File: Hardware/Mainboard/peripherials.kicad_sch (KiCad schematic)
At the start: 2 parts, among them J14 Conn_02x03_Odd_Even, J15 Conn_02x03_Odd_Even

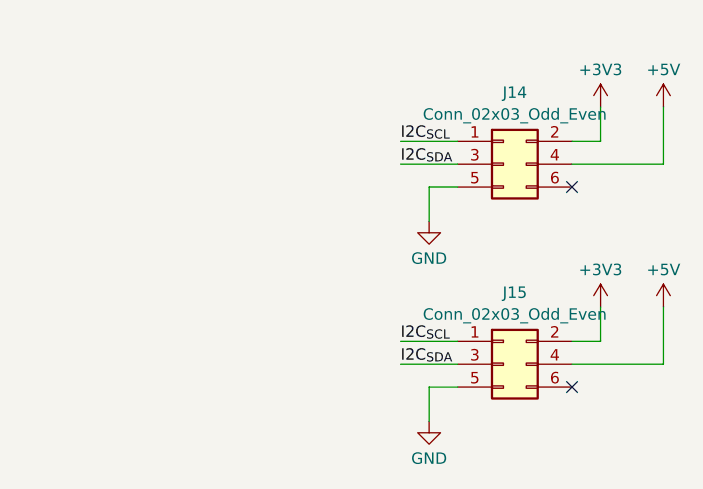
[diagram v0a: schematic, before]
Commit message: Adds more work on the mainboard schematic
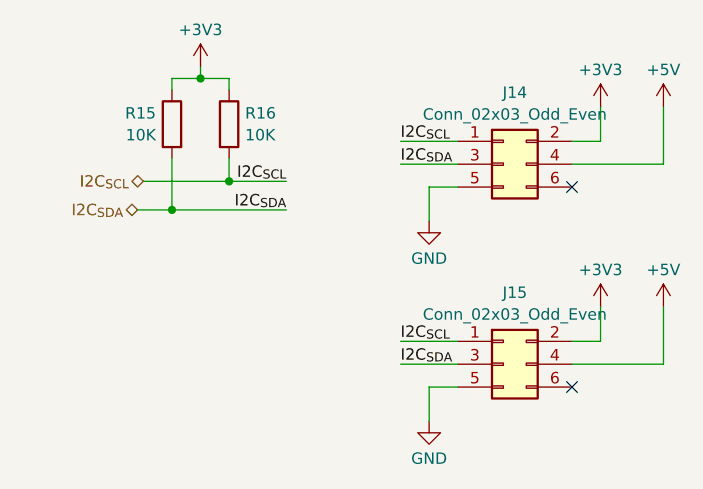
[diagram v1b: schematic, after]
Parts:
- added R15, R16: 10K, Resistor_SMD:R_0603_1608Metric_Pad0.98x0.95mm_HandSolder, symbol Device:R
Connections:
- net +3V3: now also R15.1, R16.1
- net I2C_{SCL}: now also R16.2
- net I2C_{SDA}: now also R15.2
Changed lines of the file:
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@@
 (kicad_sch (version 20230121) (generator eeschema)
   (paper "A4")
+  (junction (at 28.575 25.4) (diameter 0) (color 0 0 0 0)
+  )
+  (junction (at 25.4 40.005) (diameter 0) (color 0 0 0 0)
+  )
+  (junction (at 31.75 36.83) (diameter 0) (color 0 0 0 0)
+  )
   (no_connect (at 69.85 37.465))
   (no_connect (at 69.85 59.69))
@@
     (stroke (width 0) (type default))
   )
+  (wire (pts (xy 25.4 26.67) (xy 25.4 25.4))
+    (stroke (width 0) (type default))
+  )
   (wire (pts (xy 69.85 34.925) (xy 80.01 34.925))
     (stroke (width 0) (type default))
@@
     (stroke (width 0) (type default))
   )
+  (wire (pts (xy 28.575 25.4) (xy 31.75 25.4))
+    (stroke (width 0) (type default))
+  )
+  (wire (pts (xy 31.75 36.83) (xy 38.1 36.83))
+    (stroke (width 0) (type default))
+  )
   (wire (pts (xy 57.15 37.465) (xy 53.975 37.465))
     (stroke (width 0) (type default))
@@
     (stroke (width 0) (type default))
   )
+  (wire (pts (xy 25.4 25.4) (xy 28.575 25.4))
+    (stroke (width 0) (type default))
+  )
+  (wire (pts (xy 31.75 34.29) (xy 31.75 36.83))
+    (stroke (width 0) (type default))
+  )
   (wire (pts (xy 80.01 50.8) (xy 80.01 57.15))
     (stroke (width 0) (type default))
   )
+  (wire (pts (xy 28.575 24.13) (xy 28.575 25.4))
+    (stroke (width 0) (type default))
+  )
+  (wire (pts (xy 25.4 40.005) (xy 38.1 40.005))
+    (stroke (width 0) (type default))
+  )
+  (wire (pts (xy 25.4 34.29) (xy 25.4 40.005))
+    (stroke (width 0) (type default))
+  )
   (wire (pts (xy 50.8 54.61) (xy 57.15 54.61))
     (stroke (width 0) (type default))
@@
     (stroke (width 0) (type default))
   )
+  (wire (pts (xy 22.225 36.83) (xy 31.75 36.83))
+    (stroke (width 0) (type default))
+  )
   (wire (pts (xy 69.85 32.385) (xy 73.025 32.385))
     (stroke (width 0) (type default))
@@
   (wire (pts (xy 69.85 54.61) (xy 73.025 54.61))
     (stroke (width 0) (type default))
+  )
+  (wire (pts (xy 31.75 26.67) (xy 31.75 25.4))
+    (stroke (width 0) (type default))
+  )
+  (wire (pts (xy 21.59 40.005) (xy 25.4 40.005))
+    (stroke (width 0) (type default))
+  )
+  (label "I2C_{SCL}" (at 38.1 36.83 180) (fields_autoplaced)
+    (effects (font (size 1.27 1.27)) (justify right bottom))
   )
   (label "I2C_{SCL}" (at 50.8 32.385 0) (fields_autoplaced)
@@
     (effects (font (size 1.27 1.27)) (justify left bottom))
   )
+  (label "I2C_{SDA}" (at 38.1 40.005 180) (fields_autoplaced)
+    (effects (font (size 1.27 1.27)) (justify right bottom))
+  )
   (label "I2C_{SCL}" (at 50.8 54.61 0) (fields_autoplaced)
     (effects (font (size 1.27 1.27)) (justify left bottom))
@@
   (label "I2C_{SDA}" (at 50.8 34.925 0) (fields_autoplaced)
     (effects (font (size 1.27 1.27)) (justify left bottom))
+  )
+  (hierarchical_label "I2C_{SDA}" (shape bidirectional) (at 21.59 40.005 180) (fields_autoplaced)
+    (effects (font (size 1.27 1.27)) (justify right))
+  )
+  (hierarchical_label "I2C_{SCL}" (shape bidirectional) (at 22.225 36.83 180) (fields_autoplaced)
+    (effects (font (size 1.27 1.27)) (justify right))
   )
   (symbol (lib_id "power:+3V3") (at 73.025 28.575 0) (unit 1)
@@
     )
   )
+  (symbol (lib_id "power:+3V3") (at 28.575 24.13 0) (unit 1)
+    (in_bom yes) (on_board yes) (dnp no) (fields_autoplaced)
+    (property "Reference" "#PWR077" (at 28.575 27.94 0)
+      (effects (font (size 1.27 1.27)) hide)
+    )
+    (property "Value" "+3V3" (at 28.575 19.9969 0)
+      (effects (font (size 1.27 1.27)))
+    )
+    (property "Footprint" "" (at 28.575 24.13 0)
+      (effects (font (size 1.27 1.27)) hide)
+    )
+    (property "Datasheet" "" (at 28.575 24.13 0)
+      (effects (font (size 1.27 1.27)) hide)
+    )
+    (pin "1")
+    (instances
+      (project "Mainboard"
+        (path "/e63e39d7-6ac0-4ffd-8aa3-1841a4541b55/4cb22642-07ad-451c-aff9-3a7f1441fcd4"
+          (reference "#PWR077") (unit 1)
+        )
+      )
+    )
+  )
+  (symbol (lib_id "Device:R") (at 25.4 30.48 0) (mirror y) (unit 1)
+    (in_bom yes) (on_board yes) (dnp no)
+    (property "Reference" "R15" (at 23.622 29.2679 0)
+      (effects (font (size 1.27 1.27)) (justify left))
+    )
+    (property "Value" "10K" (at 23.622 31.6921 0)
+      (effects (font (size 1.27 1.27)) (justify left))
+    )
+    (property "Footprint" "Resistor_SMD:R_0603_1608Metric_Pad0.98x0.95mm_HandSolder" (at 27.178 30.48 90)
+      (effects (font (size 1.27 1.27)) hide)
+    )
+    (property "Datasheet" "~" (at 25.4 30.48 0)
+      (effects (font (size 1.27 1.27)) hide)
+    )
+    (pin "2")
+    (pin "1")
+    (instances
+      (project "Mainboard"
+        (path "/e63e39d7-6ac0-4ffd-8aa3-1841a4541b55/4cb22642-07ad-451c-aff9-3a7f1441fcd4"
+          (reference "R15") (unit 1)
+        )
+      )
+    )
+  )
   (symbol (lib_id "power:GND") (at 53.975 41.275 0) (unit 1)
     (in_bom yes) (on_board yes) (dnp no) (fields_autoplaced)
@@
         )
       )
+    )
+  )
+  (symbol (lib_id "Device:R") (at 31.75 30.48 0) (unit 1)
+    (in_bom yes) (on_board yes) (dnp no) (fields_autoplaced)
+    (property "Reference" "R16" (at 33.528 29.2679 0)
+      (effects (font (size 1.27 1.27)) (justify left))
+    )
+    (property "Value" "10K" (at 33.528 31.6921 0)
+      (effects (font (size 1.27 1.27)) (justify left))
+    )
+    (property "Footprint" "Resistor_SMD:R_0603_1608Metric_Pad0.98x0.95mm_HandSolder" (at 29.972 30.48 90)
+      (effects (font (size 1.27 1.27)) hide)
+    )
+    (property "Datasheet" "~" (at 31.75 30.48 0)
+      (effects (font (size 1.27 1.27)) hide)
+    )
+    (pin "2")
+    (pin "1")
+    (instances
+      (project "Mainboard"
+        (path "/e63e39d7-6ac0-4ffd-8aa3-1841a4541b55/4cb22642-07ad-451c-aff9-3a7f1441fcd4"
+          (reference "R16") (unit 1)
+        )
+      )
